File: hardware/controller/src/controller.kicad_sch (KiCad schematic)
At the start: 40 parts, among them J1 To Display, J2 Display, J3 Barrel_Jack_Switch, J4 Program, J5 JTAG, SW1 RESET, SW2 BTN1, SW3 BTN1, U1 ESP32-WROOM-E, U2 XL1509-5.0, U3 XL1509-3.3, U4 RS0102YH8, U5 ESP32-S3-WROOM-1

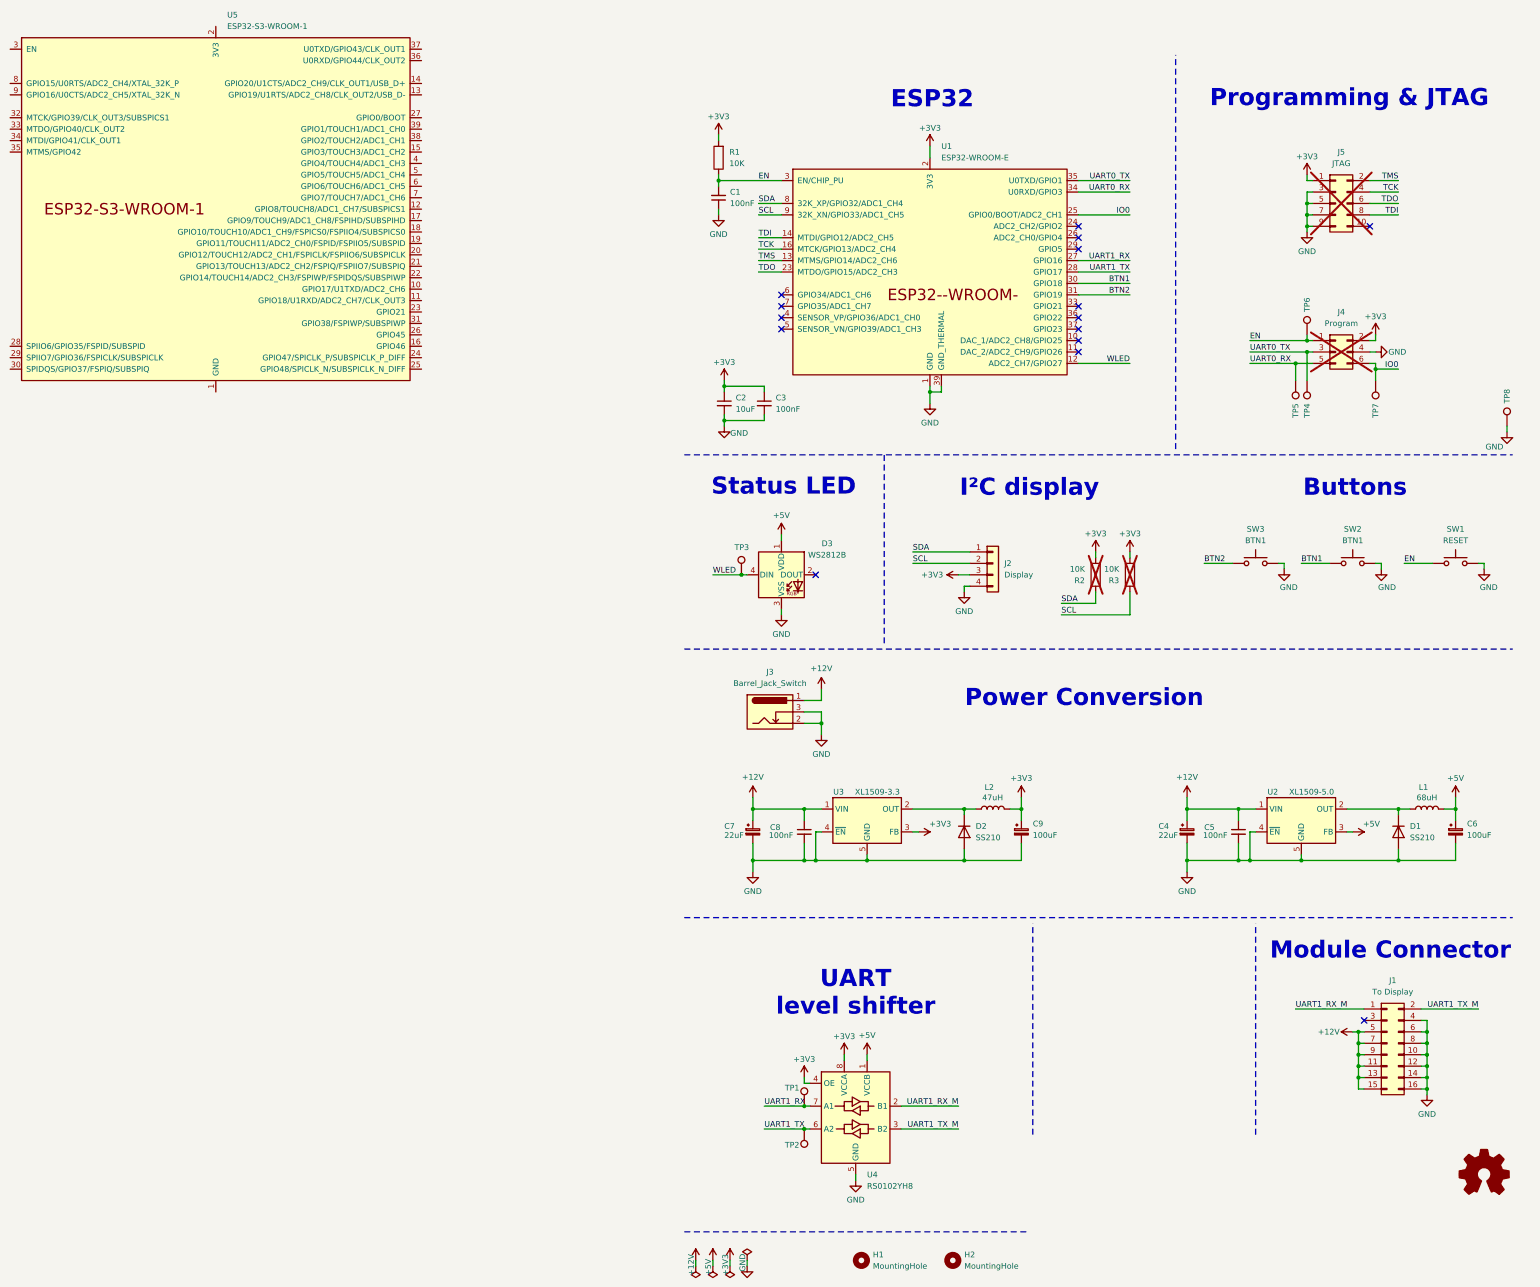
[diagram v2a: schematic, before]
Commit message: Design controller as a top connector board.
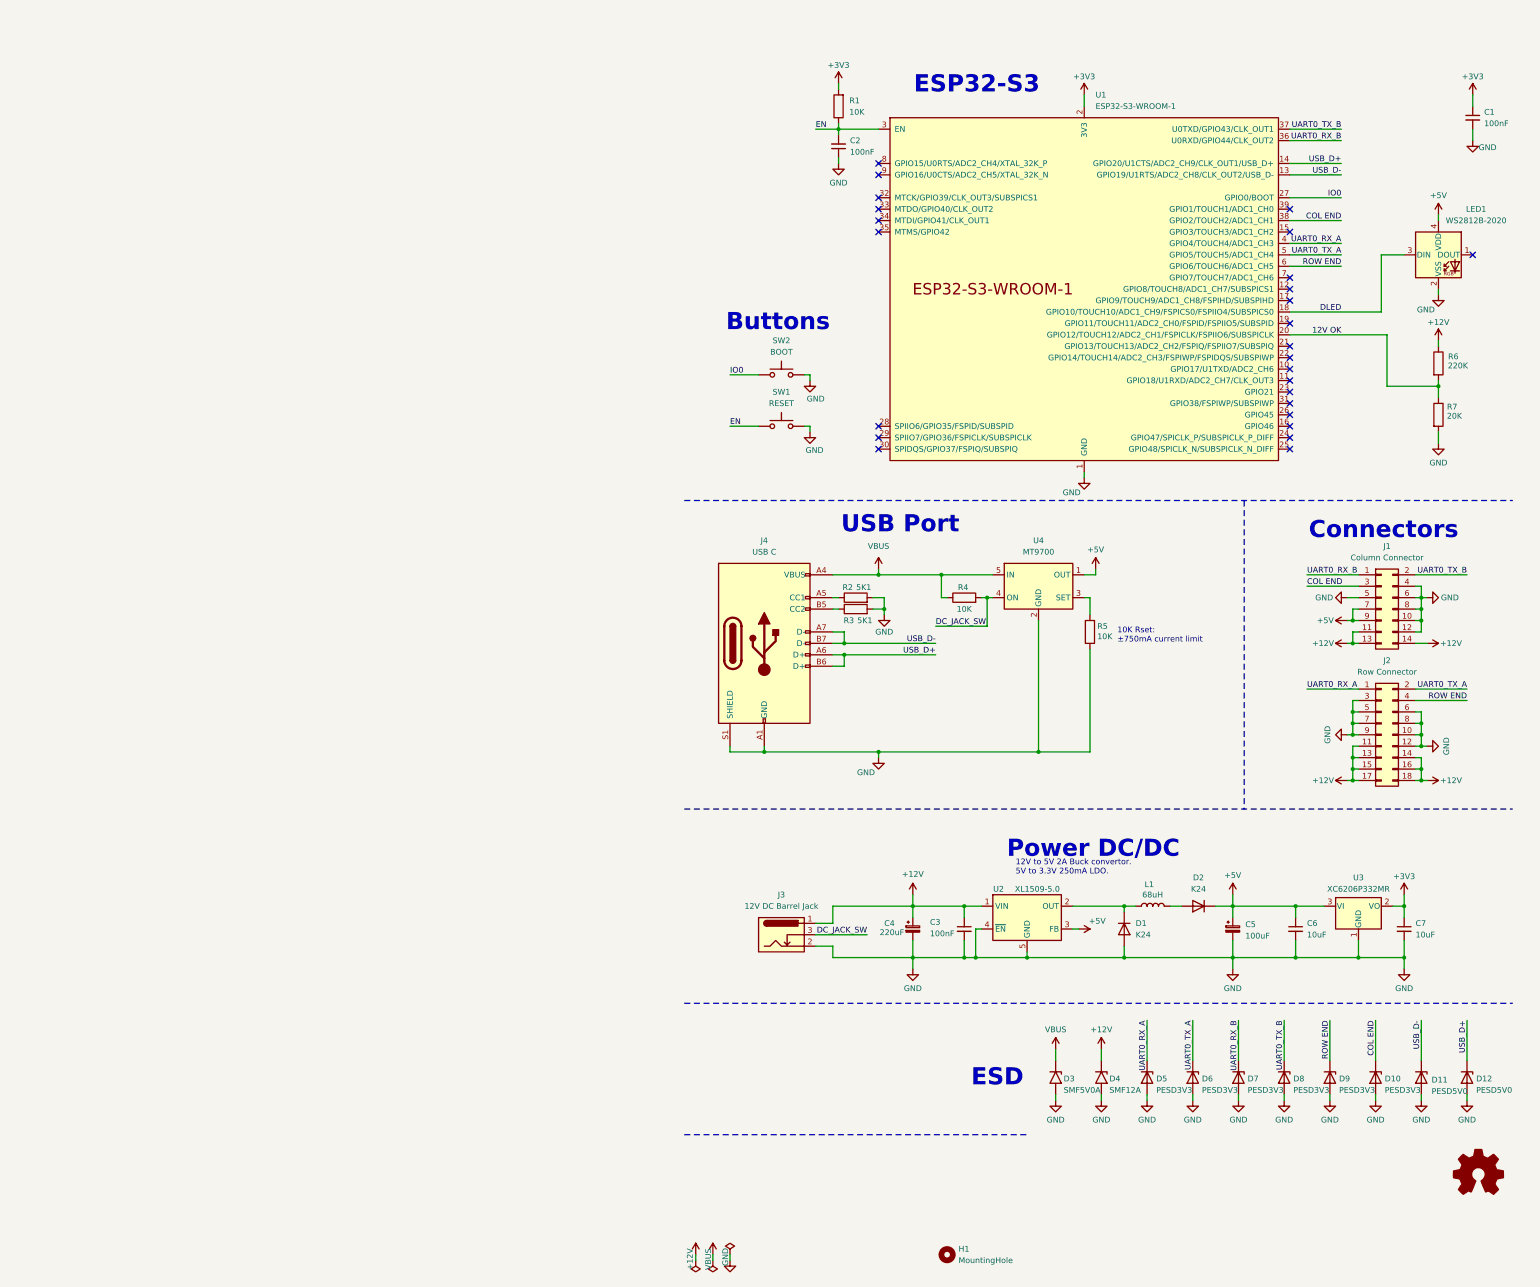
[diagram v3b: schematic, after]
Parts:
- removed C5, C8: 100nF, Capacitor_SMD:C_0805_2012Metric, symbol Device:C_Small
- removed C6, C9: 100uF, Capacitor_Tantalum_SMD:CP_EIA-3528-21_Kemet-B, symbol Device:C_Polarized_Small
- removed C7: 22uF, Capacitor_SMD:CP_Elec_5x5.4, symbol Device:C_Polarized_Small
- removed D3: WS2812B, LED_SMD:LED_WS2812B_PLCC4_5.0x5.0mm_P3.2mm, symbol LED:WS2812B
- removed H2: MountingHole, MountingHole:MountingHole_2.7mm_M2.5, symbol Mechanical:MountingHole
- removed J1: To Display, Connector_IDC:IDC-Header_2x08_P2.54mm_Vertical, symbol Connector_Generic:Conn_02x08_Odd_Even
- removed J2: Display, Connector_PinSocket_2.54mm:PinSocket_1x04_P2.54mm_Vertical, symbol Connector_Generic:Conn_01x04
- removed J4: Program, BoxHeader:2x03 Box Header 1.27, symbol Connector_Generic:Conn_02x03_Odd_Even
- removed J5: JTAG, BoxHeader:2x05 Box Header 1.27, symbol Connector_Generic:Conn_02x05_Odd_Even
- removed L2: 47uH, Inductor_SMD:L_Sunlord_SWPA6045S, symbol Device:L
- removed SW3: BTN1, Button_Switch_SMD:SW_SPST_PTS645, symbol Switch:SW_Push
- removed TP1, TP2, TP3, TP4, TP5, TP6, TP7, TP8: ~, TestPoint:TestPoint_Pad_D1.5mm, symbol Connector:TestPoint
- removed U1: ESP32-WROOM-E, PCM_Espressif:ESP32-WROOM-32E, symbol PCM_Espressif:ESP32-WROOM-E
- removed U3: XL1509-3.3, Package_SO:SOIC-8_3.9x4.9mm_P1.27mm, symbol Regulator_Switching:XL1509-5.0
- removed U4: RS0102YH8, Package_TO_SOT_SMD:SOT-23-8, symbol RS0102Y:RS0102Y
- removed U5: ESP32-S3-WROOM-1, PCM_Espressif:ESP32-S3-WROOM-1, symbol PCM_Espressif:ESP32-S3-WROOM-1
- added C5: 100uF, Capacitor_Tantalum_SMD:CP_EIA-3528-21_Kemet-B, symbol Device:C_Polarized_Small
- added C6, C7: 10uF, Capacitor_SMD:C_0805_2012Metric, symbol Device:C_Small
- added D10, D5, D6, D7, D8, D9: PESD3V3, Diode_SMD:D_SOD-523, symbol Device:D_Zener
- added D11, D12: PESD5V0, Diode_SMD:D_SOD-523, symbol Device:D_Zener
- added D3: SMF5V0A, Diode_SMD:D_SMF, symbol Diode:SMF5V0A
- added D4: SMF12A, Diode_SMD:D_SMF, symbol Diode:SMF12A
- added J1: Column Connector, Connector_Samtec_HLE_SMD:Samtec_HLE-107-02-xxx-DV-BE-A_2x07_P2.54mm_Horizontal, symbol Connector_Generic:Conn_02x07_Odd_Even
- added J2: Row Connector, Connector_IDC:IDC-Header_2x09_P2.54mm_Vertical, symbol Connector_Generic:Conn_02x09_Odd_Even
- added J4: USB C, USB-C-connector:MC-803LS-HXXX, symbol Connector:USB_C_Receptacle_USB2.0_14P
- added LED1: WS2812B-2020, LED_SMD:LED_WS2812B-2020_PLCC4_2.0x2.0mm, symbol LED:WS2812B-2020
- added R4, R5: 10K, Resistor_SMD:R_0603_1608Metric, symbol Device:R
- added R6: 220K, Resistor_SMD:R_0603_1608Metric, symbol Device:R
- added R7: 20K, Resistor_SMD:R_0603_1608Metric, symbol Device:R
- added U1: ESP32-S3-WROOM-1, PCM_Espressif:ESP32-S3-WROOM-1, symbol PCM_Espressif:ESP32-S3-WROOM-1
- added U3: XC6206P332MR, Package_TO_SOT_SMD:SOT-23-3, symbol Regulator_Linear:XC6206PxxxMR
- added U4: MT9700, Package_TO_SOT_SMD:SOT-23-5, symbol Power_Management:AAT4610BIGV-1-T1
- C2: value 10uF -> 100nF
- C4: value 22uF -> 220uF; footprint Capacitor_SMD:CP_Elec_5x5.4 -> Capacitor_SMD:CP_Elec_6.3x7.7
- D1, D2: value SS210 -> K24; footprint Diode_SMD:D_SMA -> Diode_SMD:D_SMF; LCSC C14996 -> C5199107
- J3: value Barrel_Jack_Switch -> 12V DC Barrel Jack; footprint Connector_BarrelJack:BarrelJack_CLIFF_FC681465S_SMT_Horizontal -> DC-jack-connector:DC-012A-25A; LCSC C319133 -> C2880578
- R1: footprint Resistor_SMD:R_0805_2012Metric -> Resistor_SMD:R_0603_1608Metric
- R2, R3: value 10K -> 5K1; footprint Resistor_SMD:R_0805_2012Metric -> Resistor_SMD:R_0603_1608Metric; now fitted; now in the parts list
- SW1: footprint Button_Switch_SMD:SW_SPST_PTS645 -> Button_Switch_SMD:SW_SPST_EVQP7C; LCSC C5340120 -> C528965
- SW2: value BTN1 -> BOOT; footprint Button_Switch_SMD:SW_SPST_PTS645 -> Button_Switch_SMD:SW_SPST_EVQP7C; LCSC C5340120 -> C528965
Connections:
- net BTN1 is gone; now on net IO0: SW2.1
- net SCL is gone; now on net GND: R3.2
- net SDA is gone; now on net GND: R2.2
- net +12V: now also C3.1, D4.1 (A1), J1.11 (Pin_11), J1.13 (Pin_13), J1.14 (Pin_14), J2.11 (Pin_11), J2.13 (Pin_13), J2.14 (Pin_14), J2.15 (Pin_15), J2.16 (Pin_16), J2.17 (Pin_17), J2.18 (Pin_18), R6.1
- net +3V3: now also C1.1, C7.1, U1.2 (3V3), U3.2 (VO); no longer C2.1, C3.1, R2.1, R3.1
- net +5V: now also D2.1 (K), C5.1, C6.1, J1.7 (Pin_7), J1.9 (Pin_9), LED1.4 (VDD), U3.3 (VI), U4.1 (OUT); no longer L1.2
- net EN: now also C2.2, U1.3 (EN); no longer C1.2
- net GND: now also C1.2, C2.1, C5.2, C6.2, C7.2, D10.2 (A), D11.2 (A), D12.2 (A), D3.2 (A2), D4.2 (A2), D5.2 (A), D6.2 (A), D7.2 (A), D8.2 (A), D9.2 (A), J1.10 (Pin_10), J1.12 (Pin_12), J1.4 (Pin_4), J1.5 (Pin_5), J1.6 (Pin_6), J1.8 (Pin_8), J2.10 (Pin_10), J2.12 (Pin_12), J2.3 (Pin_3), J2.5 (Pin_5), J2.6 (Pin_6), J2.7 (Pin_7), J2.8 (Pin_8), J2.9 (Pin_9), J4.A1 (GND), J4.A12 (GND), J4.B1 (GND), J4.B12 (GND), J4.S1 (SHIELD), LED1.2 (VSS), R5.1, R7.2, U1.1 (GND), U1.40 (GND), U1.41 (GND), U3.1 (GND), U4.2 (GND); no longer C1.1, C2.2, D2.2 (A), J3.3
- net IO0: now also U1.27 (GPIO0/BOOT)
- new net: R5.2, U4.3 (SET)
- new net: J4.A5 (CC1), R2.1
- new net: D2.2 (A), L1.2
- new net: J4.B5 (CC2), R3.1
- new net 12V OK: R6.2, R7.1, U1.20 (GPIO12/TOUCH12/ADC2_CH1/FSPICLK/FSPIIO6/SUBSPICLK)
- new net COL END: D10.1 (K), J1.3 (Pin_3), U1.38 (GPIO2/TOUCH2/ADC1_CH1)
- new net DC_JACK_SW: J3.3, R4.2, U4.4 (ON)
- new net DLED: LED1.3 (DIN), U1.18 (GPIO10/TOUCH10/ADC1_CH9/FSPICS0/FSPIIO4/SUBSPICS0)
- new net ROW END: D9.1 (K), J2.4 (Pin_4), U1.6 (GPIO6/TOUCH6/ADC1_CH5)
- new net UART0_RX_A: D5.1 (K), J2.1 (Pin_1), U1.4 (GPIO4/TOUCH4/ADC1_CH3)
- new net UART0_RX_B: D7.1 (K), J1.1 (Pin_1), U1.36 (U0RXD/GPIO44/CLK_OUT2)
- new net UART0_TX_A: D6.1 (K), J2.2 (Pin_2), U1.5 (GPIO5/TOUCH5/ADC1_CH4)
- new net UART0_TX_B: D8.1 (K), J1.2 (Pin_2), U1.37 (U0TXD/GPIO43/CLK_OUT1)
- new net USB_D+: D12.1 (K), J4.A6 (D+), J4.B6 (D+), U1.14 (GPIO20/U1CTS/ADC2_CH9/CLK_OUT1/USB_D+)
- new net USB_D-: D11.1 (K), J4.A7 (D-), J4.B7 (D-), U1.13 (GPIO19/U1RTS/ADC2_CH8/CLK_OUT2/USB_D-)
- new net VBUS: D3.1 (A1), J4.A4 (VBUS), J4.A9 (VBUS), J4.B4 (VBUS), J4.B9 (VBUS), R4.1, U4.5 (IN)
- no-connect marks 15 -> 26
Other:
- note added: "10K Rset: ±750mA current limit"
- note added: "12V to 5V 2A Buck convertor. 5V to 3.3V 250mA LDO."
- note added: "Connectors"
- note added: "ESD"
- note added: "ESP32-S3"
- note added: "Power DC/DC"
- note added: "USB Port"
- note removed: "ESP32"
- note removed: "I²C display"
- note removed: "Module Connector"
- note removed: "Power Conversion"
- note removed: "Programming & JTAG"
- note removed: "Status LED"
- note removed: "UART level shifter"
- title: Controller -> Top Controller

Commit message: Add dynamic uart routing and bridging to controller, Remove OLED libs
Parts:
- added RX0, TX0: TestPoint, TestPoint:TestPoint_Pad_D1.5mm, symbol Connector:TestPoint
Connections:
- net UART1_TX_B: now reaches U1.24 (GPIO47/SPICLK_P/SUBSPICLK_P_DIFF)
- net UART1_TX_B: now also D8.1 (K), J1.2 (Pin_2)
- net UART1_RX_B: now reaches U1.25 (GPIO48/SPICLK_N/SUBSPICLK_N_DIFF)
- net UART1_RX_B: now also D7.1 (K), J1.1 (Pin_1)
- net COL END renamed COL START
- net ROW END renamed ROW START
- net UART0_RX_A renamed UART1_RX_A
- removed net UART0_RX_B: D7.1 (K), J1.1 (Pin_1), U1.36 (U0RXD/GPIO44/CLK_OUT2)
- net UART0_TX_A renamed UART1_TX_A
- removed net UART0_TX_B: D8.1 (K), J1.2 (Pin_2), U1.37 (U0TXD/GPIO43/CLK_OUT1)
- new net UART0_RX: RX0.1, U1.36 (U0RXD/GPIO44/CLK_OUT2)
- new net UART0_TX: TX0.1, U1.37 (U0TXD/GPIO43/CLK_OUT1)
- no-connect marks 26 -> 24
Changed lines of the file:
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@@
 	)
 	(no_connect
-		(at 147.32 100.33)
-	)
-	(no_connect
 		(at 147.32 80.01)
 	)
@@
 	)
 	(no_connect
-		(at 147.32 97.79)
-	)
-	(no_connect
 		(at 55.88 100.33)
 	)
@@
 	(wire
 		(pts
+			(xy 147.32 100.33) (xy 158.75 100.33)
+		)
+		(stroke
+			(width 0)
+			(type default)
+		)
+	)
+	(wire
+		(pts
 			(xy 151.13 130.81) (xy 162.56 130.81)
 		)
@@
 	(wire
 		(pts
+			(xy 147.32 97.79) (xy 158.75 97.79)
+		)
+		(stroke
+			(width 0)
+			(type default)
+		)
+	)
+	(wire
+		(pts
 			(xy 63.5 213.36) (xy 74.93 213.36)
 		)
@@
 		)
 	)
-	(label "ROW END"
+	(label "ROW START"
 		(at 158.75 59.69 180)
 		(fields_autoplaced yes)
@@
 		)
 	)
-	(label "COL END"
+	(label "COL START"
 		(at 151.13 130.81 0)
 		(fields_autoplaced yes)
@@
 		)
 	)
-	(label "UART0_RX_B"
+	(label "UART1_RX_B"
 		(at 151.13 128.27 0)
 		(fields_autoplaced yes)
@@
 		)
 	)
-	(label "UART0_TX_A"
+	(label "UART1_TX_A"
 		(at 158.75 57.15 180)
 		(fields_autoplaced yes)
@@
 		)
 	)
-	(label "UART0_RX_A"
+	(label "UART1_TX_B"
+		(at 158.75 97.79 180)
+		(fields_autoplaced yes)
+		(effects
+			(font
+				(size 1.27 1.27)
+			)
+			(justify right bottom)
+		)
+	)
+	(label "UART1_RX_A"
 		(at 158.75 54.61 180)
 		(fields_autoplaced yes)
@@
 		)
 	)
-	(label "UART0_RX_A"
+	(label "UART1_RX_A"
 		(at 115.57 227.33 270)
 		(fields_autoplaced yes)
@@
 		)
 	)
-	(label "UART0_TX_A"
+	(label "UART1_TX_A"
 		(at 125.73 227.33 270)
 		(fields_autoplaced yes)
@@
 		)
 	)
-	(label "UART0_TX_B"
+	(label "UART1_TX_B"
 		(at 146.05 227.33 270)
 		(fields_autoplaced yes)
@@
 		)
 	)
-	(label "COL END"
+	(label "COL START"
 		(at 158.75 49.53 180)
 		(fields_autoplaced yes)
@@
 		)
 	)
-	(label "ROW END"
+	(label "ROW START"
 		(at 186.69 156.21 180)
 		(fields_autoplaced yes)
@@
 		)
 	)
-	(label "ROW END"
+	(label "ROW START"
 		(at 156.21 227.33 270)
 		(fields_autoplaced yes)
@@
 		)
 	)
-	(label "UART0_TX_B"
+	(label "UART0_TX"
 		(at 158.75 29.21 180)
 		(fields_autoplaced yes)
@@
 		)
 	)
-	(label "UART0_TX_A"
+	(label "UART1_TX_A"
 		(at 186.69 153.67 180)
 		(fields_autoplaced yes)
@@
 		)
 	)
-	(label "COL END"
+	(label "COL START"
 		(at 166.37 227.33 270)
 		(fields_autoplaced yes)
@@
 		)
 	)
-	(label "UART0_RX_B"
+	(label "UART1_RX_B"
 		(at 135.89 227.33 270)
 		(fields_autoplaced yes)
@@
 		)
 	)
-	(label "UART0_RX_B"
+	(label "UART0_RX"
 		(at 158.75 31.75 180)
 		(fields_autoplaced yes)
@@
 		)
 	)
-	(label "UART0_RX_A"
+	(label "UART1_RX_A"
 		(at 151.13 153.67 0)
 		(fields_autoplaced yes)
@@
 		)
 	)
-	(label "UART0_TX_B"
+	(label "UART1_TX_B"
 		(at 186.69 128.27 180)
 		(fields_autoplaced yes)
@@
 		)
 	)
+	(label "UART1_RX_B"
+		(at 158.75 100.33 180)
+		(fields_autoplaced yes)
+		(effects
+			(font
+				(size 1.27 1.27)
+			)
+			(justify right bottom)
+		)
+	)
 	(symbol
 		(lib_id "Device:C_Small")
@@
 	)
 	(symbol
+		(lib_id "Connector:TestPoint")
+		(at 158.75 29.21 270)
+		(unit 1)
+		(exclude_from_sim no)
+		(in_bom yes)
+		(on_board yes)
+		(dnp no)
+		(property "Reference" "TX0"
+			(at 163.83 29.21 90)
+			(effects
+				(font
+					(size 1.27 1.27)
+				)
+				(justify left)
+			)
+		)
+		(property "Value" "TestPoint"
+			(at 163.83 30.48 90)
+			(effects
+				(font
+					(size 1.27 1.27)
+				)
+				(justify left)
+				(hide yes)
+			)
+		)
+		(property "Footprint" "TestPoint:TestPoint_Pad_D1.5mm"
+			(at 158.75 34.29 0)
+			(effects
+				(font
+					(size 1.27 1.27)
+				)
+				(hide yes)
+			)
+		)
+		(property "Datasheet" "~"
+			(at 158.75 34.29 0)
+			(effects
+				(font
+					(size 1.27 1.27)
+				)
+				(hide yes)
+			)
+		)
+		(property "Description" "test point"
+			(at 158.75 29.21 0)
+			(effects
+				(font
+					(size 1.27 1.27)
+				)
+				(hide yes)
+			)
+		)
+		(pin "1"
+		)
+		(instances
+			(project ""
+				(path "/af031611-7aa5-43e1-8885-232b80813f15"
+					(reference "TX0")
+					(unit 1)
+				)
+			)
+		)
+	)
+	(symbol
 		(lib_id "Device:D_Zener")
 		(at 156.21 240.03 270)
@@
 					(unit 1)
 				)
+			)
+		)
+	)
+	(symbol
+		(lib_id "Connector:TestPoint")
+		(at 158.75 31.75 270)
+		(unit 1)
+		(exclude_from_sim no)
+		(in_bom yes)
+		(on_board yes)
+		(dnp no)
+		(property "Reference" "RX0"
+			(at 163.83 31.75 90)
+			(effects
+				(font
+					(size 1.27 1.27)
+				)
+				(justify left)
+			)
+		)
+		(property "Value" "TestPoint"
+			(at 163.83 33.02 90)
+			(effects
+				(font
+					(size 1.27 1.27)
+				)
+				(justify left)
+				(hide yes)
+			)
+		)
+		(property "Footprint" "TestPoint:TestPoint_Pad_D1.5mm"
+			(at 158.75 36.83 0)
+			(effects
+				(font
+					(size 1.27 1.27)
+				)
+				(hide yes)
+			)
+		)
+		(property "Datasheet" "~"
+			(at 158.75 36.83 0)
+			(effects
+				(font
+					(size 1.27 1.27)
+				)
+				(hide yes)
+			)
+		)
+		(property "Description" "test point"
+			(at 158.75 31.75 0)
+			(effects
+				(font
+					(size 1.27 1.27)
+				)
+				(hide yes)
+			)
+		)
+		(pin "1"
+		)
+		(instances
+			(project "controller"
+				(path "/af031611-7aa5-43e1-8885-232b80813f15"
+					(reference "RX0")
+					(unit 1)
+				)

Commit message: Documentation Updates
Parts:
- added J5: Conn_01x02, Connector_AMASS:AMASS_XT30U-M_1x02_P5.0mm_Vertical, symbol Connector_Generic:Conn_01x02
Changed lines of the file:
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@@
+	)
+	(symbol
+		(lib_id "Connector_Generic:Conn_01x02")
+		(at 26.67 189.23 0)
+		(unit 1)
+		(exclude_from_sim no)
+		(in_bom yes)
+		(on_board yes)
+		(dnp no)
+		(fields_autoplaced yes)
+		(property "Reference" "J5"
+			(at 29.21 189.23 0)
+			(effects
+				(font
+					(size 1.27 1.27)
+				)
+				(justify left)
+			)
+		)
+		(property "Value" "Conn_01x02"
+			(at 29.21 191.77 0)
+			(effects
+				(font
+					(size 1.27 1.27)
+				)
+				(justify left)
+			)
+		)
+		(property "Footprint" "Connector_AMASS:AMASS_XT30U-M_1x02_P5.0mm_Vertical"
+			(at 26.67 189.23 0)
+			(effects
+				(font
+					(size 1.27 1.27)
+				)
+				(hide yes)
+			)
+		)
+		(property "Datasheet" "~"
+			(at 26.67 189.23 0)
+			(effects
+				(font
+					(size 1.27 1.27)
+				)
+				(hide yes)
+			)
+		)
+		(property "Description" "Generic connector, single row, 01x02, script generated (kicad-library-utils/schlib/autogen/connector/)"
+			(at 26.67 189.23 0)
+			(effects
+				(font
+					(size 1.27 1.27)
+				)
+				(hide yes)
+			)
+		)
+		(pin "2"
+		)
+		(pin "1"
+		)
+		(instances
+			(project ""
+				(path "/af031611-7aa5-43e1-8885-232b80813f15"
+					(reference "J5")
+					(unit 1)
+				)
+			)
+		)
 	)
 	(symbol
